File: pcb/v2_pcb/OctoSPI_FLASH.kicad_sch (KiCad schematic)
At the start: 5 parts, among them U5 MX25U51279GXDR00

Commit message: fnish micro sd card
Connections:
- net OCTOSPI_IO1: now also U5.D2 (SO/SIO1)
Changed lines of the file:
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@@
+	(wire
+		(pts
+			(xy 81.28 91.44) (xy 133.35 91.44)
+		)
+		(stroke
+			(width 0)
+			(type default)
+		)
+	)
 	(wire
 		(pts

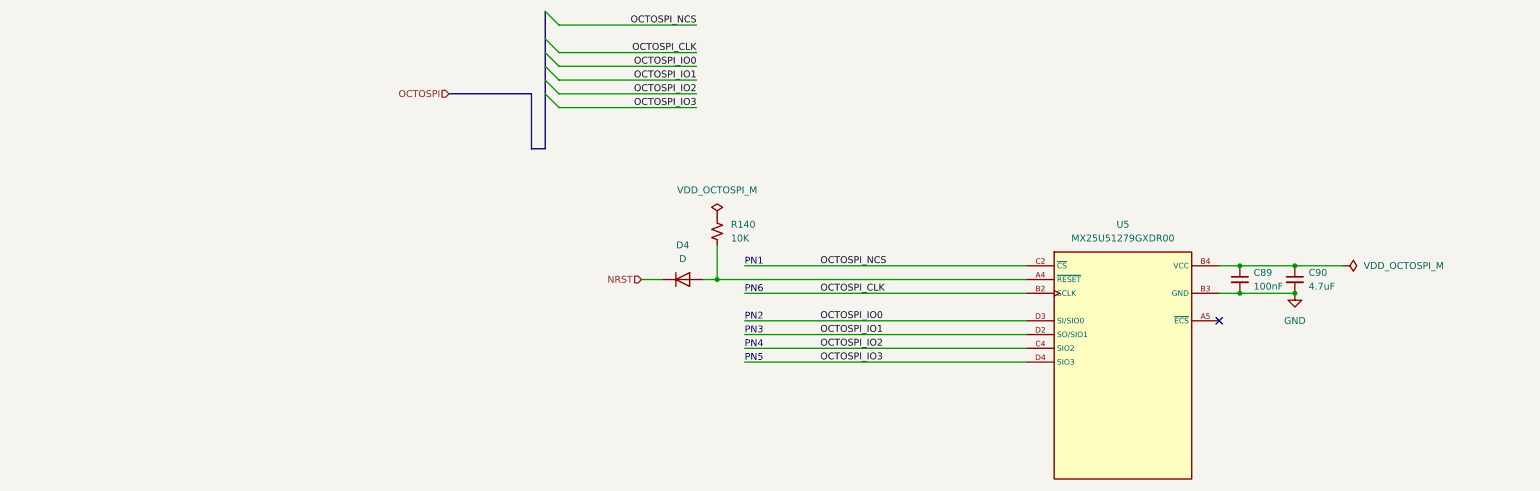
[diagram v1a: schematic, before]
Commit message: done with max17320
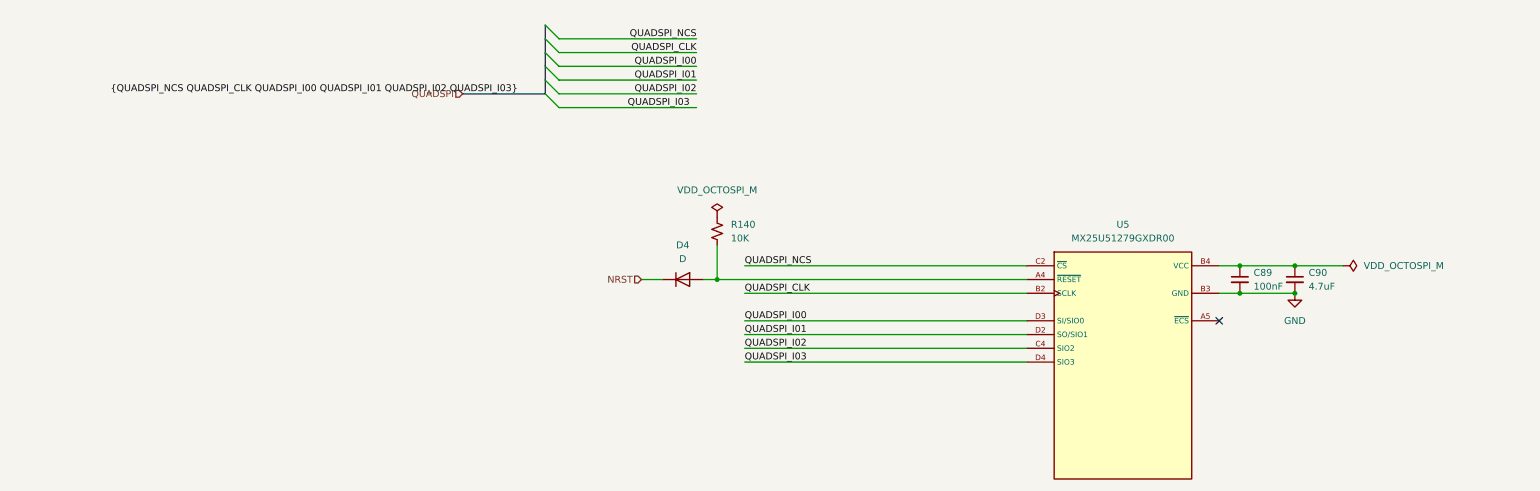
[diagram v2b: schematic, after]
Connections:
- net OCTOSPI_CLK renamed QUADSPI_CLK
- net OCTOSPI_IO0 renamed QUADSPI_I00
- net OCTOSPI_IO1 renamed QUADSPI_I01
- net OCTOSPI_IO2 renamed QUADSPI_I02
- net OCTOSPI_IO3 renamed QUADSPI_I03
- net OCTOSPI_NCS renamed QUADSPI_NCS
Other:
- note removed: "PN1"
- note removed: "PN2"
- note removed: "PN3"
- note removed: "PN4"
- note removed: "PN5"
- note removed: "PN6"
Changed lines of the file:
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@@
 	(generator_version "10.0")
 	(paper "A4")
-	(text "PN3"
-		(exclude_from_sim no)
-		(at 81.28 91.44 0)
-		(effects
-			(font
-				(size 1.27 1.27)
-			)
-			(justify left bottom)
-		)
-	)
-	(text "PN1"
-		(exclude_from_sim no)
-		(at 81.28 78.74 0)
-		(effects
-			(font
-				(size 1.27 1.27)
-			)
-			(justify left bottom)
-		)
-	)
-	(text "PN2\n"
-		(exclude_from_sim no)
-		(at 81.28 88.9 0)
-		(effects
-			(font
-				(size 1.27 1.27)
-			)
-			(justify left bottom)
-		)
-	)
-	(text "PN5"
-		(exclude_from_sim no)
-		(at 81.28 96.52 0)
-		(effects
-			(font
-				(size 1.27 1.27)
-			)
-			(justify left bottom)
-		)
-	)
-	(text "PN6\n"
-		(exclude_from_sim no)
-		(at 81.28 83.82 0)
-		(effects
-			(font
-				(size 1.27 1.27)
-			)
-			(justify left bottom)
-		)
-	)
-	(text "PN4"
-		(exclude_from_sim no)
-		(at 81.28 93.98 0)
-		(effects
-			(font
-				(size 1.27 1.27)
-			)
-			(justify left bottom)
-		)
-	)
 	(junction
 		(at 76.2 81.28)
@@
 	)
 	(bus_entry
-		(at 46.99 34.29)
-		(size -2.54 -2.54)
-		(stroke
-			(width 0)
-			(type default)
-		)
-	)
-	(wire
-		(pts
-			(xy 46.99 34.29) (xy 72.39 34.29)
+		(at 46.99 36.83)
+		(size -2.54 -2.54)
+		(stroke
+			(width 0)
+			(type default)
+		)
+	)
+	(wire
+		(pts
+			(xy 46.99 36.83) (xy 72.39 36.83)
 		)
 		(stroke
@@
 	(bus
 		(pts
-			(xy 26.67 46.99) (xy 41.91 46.99)
+			(xy 29.21 46.99) (xy 44.45 46.99)
 		)
 		(stroke
@@
 		)
 	)
+	(wire
+		(pts
+			(xy 81.28 83.82) (xy 133.35 83.82)
+		)
+		(stroke
+			(width 0)
+			(type default)
+		)
+	)
+	(wire
+		(pts
+			(xy 81.28 78.74) (xy 133.35 78.74)
+		)
+		(stroke
+			(width 0)
+			(type default)
+		)
+	)
+	(wire
+		(pts
+			(xy 62.23 81.28) (xy 66.04 81.28)
+		)
+		(stroke
+			(width 0)
+			(type default)
+		)
+	)
+	(wire
+		(pts
+			(xy 46.99 49.53) (xy 72.39 49.53)
+		)
+		(stroke
+			(width 0)
+			(type default)
+		)
+	)
+	(wire
+		(pts
+			(xy 81.28 88.9) (xy 133.35 88.9)
+		)
+		(stroke
+			(width 0)
+			(type default)
+		)
+	)
+	(wire
+		(pts
+			(xy 172.72 78.74) (xy 182.88 78.74)
+		)
+		(stroke
+			(width 0)
+			(type default)
+		)
+	)
+	(wire
+		(pts
+			(xy 46.99 46.99) (xy 72.39 46.99)
+		)
+		(stroke
+			(width 0)
+			(type default)
+		)
+	)
+	(wire
+		(pts
+			(xy 73.66 81.28) (xy 76.2 81.28)
+		)
+		(stroke
+			(width 0)
+			(type default)
+		)
+	)
 	(bus
 		(pts
-			(xy 44.45 57.15) (xy 44.45 31.75)
+			(xy 44.45 34.29) (xy 44.45 46.99)
 		)
 		(stroke
 			(width 0.508)
-			(type default)
+			(type solid)
 			(color 173 188 231 1)
 		)
@@
 	(wire
 		(pts
-			(xy 81.28 83.82) (xy 133.35 83.82)
-		)
-		(stroke
-			(width 0)
-			(type default)
-		)
-	)
-	(wire
-		(pts
-			(xy 81.28 78.74) (xy 133.35 78.74)
-		)
-		(stroke
-			(width 0)
-			(type default)
-		)
-	)
-	(wire
-		(pts
-			(xy 62.23 81.28) (xy 66.04 81.28)
-		)
-		(stroke
-			(width 0)
-			(type default)
-		)
-	)
-	(wire
-		(pts
-			(xy 46.99 49.53) (xy 72.39 49.53)
-		)
-		(stroke
-			(width 0)
-			(type default)
-		)
-	)
-	(bus
-		(pts
-			(xy 44.45 57.15) (xy 41.91 57.15)
-		)
-		(stroke
-			(width 0.508)
-			(type default)
-			(color 173 188 231 1)
-		)
-	)
-	(wire
-		(pts
-			(xy 81.28 88.9) (xy 133.35 88.9)
-		)
-		(stroke
-			(width 0)
-			(type default)
-		)
-	)
-	(wire
-		(pts
-			(xy 172.72 78.74) (xy 182.88 78.74)
-		)
-		(stroke
-			(width 0)
-			(type default)
-		)
-	)
-	(wire
-		(pts
-			(xy 46.99 46.99) (xy 72.39 46.99)
-		)
-		(stroke
-			(width 0)
-			(type default)
-		)
-	)
-	(wire
-		(pts
-			(xy 73.66 81.28) (xy 76.2 81.28)
-		)
-		(stroke
-			(width 0)
-			(type default)
-		)
-	)
-	(wire
-		(pts
 			(xy 168.91 78.74) (xy 172.72 78.74)
 		)
@@
 		)
 	)
-	(bus
-		(pts
-			(xy 41.91 57.15) (xy 41.91 46.99)
-		)
-		(stroke
-			(width 0.508)
-			(type default)
-			(color 173 188 231 1)
-		)
-	)
-	(label "OCTOSPI_IO1"
+	(label "QUADSPI_I01"
 		(at 72.39 44.45 180)
 		(effects
@@
 		)
 	)
-	(label "OCTOSPI_NCS"
-		(at 95.25 78.74 0)
-		(effects
-			(font
-				(size 1.27 1.27)
-			)
-			(justify left bottom)
-		)
-	)
-	(label "OCTOSPI_IO2"
+	(label "QUADSPI_NCS"
+		(at 81.28 78.74 0)
+		(effects
+			(font
+				(size 1.27 1.27)
+			)
+			(justify left bottom)
+		)
+	)
+	(label "{QUADSPI_NCS QUADSPI_CLK QUADSPI_I00 QUADSPI_I01 QUADSPI_I02 QUADSPI_I03}"
+		(at 39.37 46.99 180)
+		(effects
+			(font
+				(size 1.27 1.27)
+			)
+			(justify right bottom)
+		)
+	)
+	(label "QUADSPI_I02"
 		(at 72.39 46.99 180)
 		(effects
@@
 		)
 	)
-	(label "OCTOSPI_IO3"
-		(at 95.25 96.52 0)
-		(effects
-			(font
-				(size 1.27 1.27)
-			)
-			(justify left bottom)
-		)
-	)
-	(label "OCTOSPI_IO0"
-		(at 95.25 88.9 0)
-		(effects
-			(font
-				(size 1.27 1.27)
-			)
-			(justify left bottom)
-		)
-	)
-	(label "OCTOSPI_CLK"
-		(at 95.25 83.82 0)
-		(effects
-			(font
-				(size 1.27 1.27)
-			)
-			(justify left bottom)
-		)
-	)
-	(label "OCTOSPI_CLK"
+	(label "QUADSPI_I03"
+		(at 81.28 96.52 0)
+		(effects
+			(font
+				(size 1.27 1.27)
+			)
+			(justify left bottom)
+		)
+	)
+	(label "QUADSPI_I00"
+		(at 81.28 88.9 0)
+		(effects
+			(font
+				(size 1.27 1.27)
+			)
+			(justify left bottom)
+		)
+	)
+	(label "QUADSPI_CLK"
+		(at 81.28 83.82 0)
+		(effects
+			(font
+				(size 1.27 1.27)
+			)
+			(justify left bottom)
+		)
+	)
+	(label "QUADSPI_CLK"
 		(at 72.39 39.37 180)
 		(effects
@@
 		)
 	)
-	(label "OCTOSPI_NCS"
-		(at 72.39 34.29 180)
-		(effects
-			(font
-				(size 1.27 1.27)
-			)
-			(justify right bottom)
-		)
-	)
-	(label "OCTOSPI_IO0"
+	(label "QUADSPI_NCS"
+		(at 72.39 36.83 180)
+		(effects
+			(font
+				(size 1.27 1.27)
+			)
+			(justify right bottom)
+		)
+	)
+	(label "QUADSPI_I00"
 		(at 72.39 41.91 180)
 		(effects
@@
 		)
 	)
-	(label "OCTOSPI_IO1"
-		(at 95.25 91.44 0)
-		(effects
-			(font
-				(size 1.27 1.27)
-			)
-			(justify left bottom)
-		)
-	)
-	(label "OCTOSPI_IO2"
-		(at 95.25 93.98 0)
-		(effects
-			(font
-				(size 1.27 1.27)
-			)
-			(justify left bottom)
-		)
-	)
-	(label "OCTOSPI_IO3"
-		(at 72.39 49.53 180)
-		(effects
-			(font
-				(size 1.27 1.27)
-			)
-			(justify right bottom)
-		)
-	)
-	(hierarchical_label "OCTOSPI"
+	(label "QUADSPI_I01"
+		(at 81.28 91.44 0)
+		(effects
+			(font
+				(size 1.27 1.27)
+			)
+			(justify left bottom)
+		)
+	)
+	(label "QUADSPI_I02"
+		(at 81.28 93.98 0)
+		(effects
+			(font
+				(size 1.27 1.27)
+			)
+			(justify left bottom)
+		)
+	)
+	(label "QUADSPI_I03"
+		(at 71.12 49.53 180)
+		(effects
+			(font
+				(size 1.27 1.27)
+			)
+			(justify right bottom)
+		)
+	)
+	(hierarchical_label "QUADSPI"
 		(shape input)
-		(at 26.67 46.99 180)
-		(effects
-			(font
+		(at 29.21 46.99 180)
+		(effects
+			(font

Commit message: add rpls for 1v8, 5v
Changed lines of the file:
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@@
 			)
 		)
-		(property "Value" "VDD_OCTOSPI_M"
+		(property "Value" "+1V8_RUN"
 			(at 76.2 64.77 0)
 			(show_name no)
@@
 			)
 		)
-		(property "Value" "VDD_OCTOSPI_M"
+		(property "Value" "+1V8_RUN"
 			(at 195.58 78.7399 90)
 			(show_name no)

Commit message: pcb done
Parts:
- removed D4: D, symbol Device:D
- added C305: 100nF, Capacitor_SMD:C_0402_1005Metric, symbol Device:C_Small
- added D4: BAT54H, Diode_SMD:D_SOD-323, symbol Device:D_Schottky_Small
- added R303: 10k, Resistor_SMD:R_0402_1005Metric, symbol Device:R_Small_US
- C89: footprint (none) -> Capacitor_SMD:C_0402_1005Metric
- C90: footprint (none) -> Capacitor_SMD:C_0603_1608Metric
- R140: value 10K -> 10k; footprint (none) -> Resistor_SMD:R_0402_1005Metric
- U5: footprint MX66UW1G45GXDI00:BGA24C100P5X5_800X600X120 -> noob:BGA24C100P5X5_800X600X120; MPN (none) -> MX25U51279GXDR00; Manufacturer (none) -> Macronix
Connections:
- net QUADSPI_NCS is gone; now on net FLASH_NCS: U5.C2 (~{CS})
- net GND: now also C305.2
- net FLASH_NCS: now reaches R140.2
- net FLASH_NCS: no longer U5.A4 (~{RESET})
- net +1V8_RUN: now reaches C89.1, C90.1, U5.B4 (VCC)
- net +1V8_RUN: now also R140.1, D4.1 (K), R303.1
- net QUADSPI_CLK renamed FLASH_CLK
- net QUADSPI_I00 renamed FLASH_IO0
- net QUADSPI_I01 renamed FLASH_IO1
- net QUADSPI_I02 renamed FLASH_IO2
- net QUADSPI_I03 renamed FLASH_IO3
- new net FLASH_RESET_N: C305.1, D4.2 (A), R303.2, U5.A4 (~{RESET})
- no-connect marks 1 -> 15
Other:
- moved on the sheet: U5

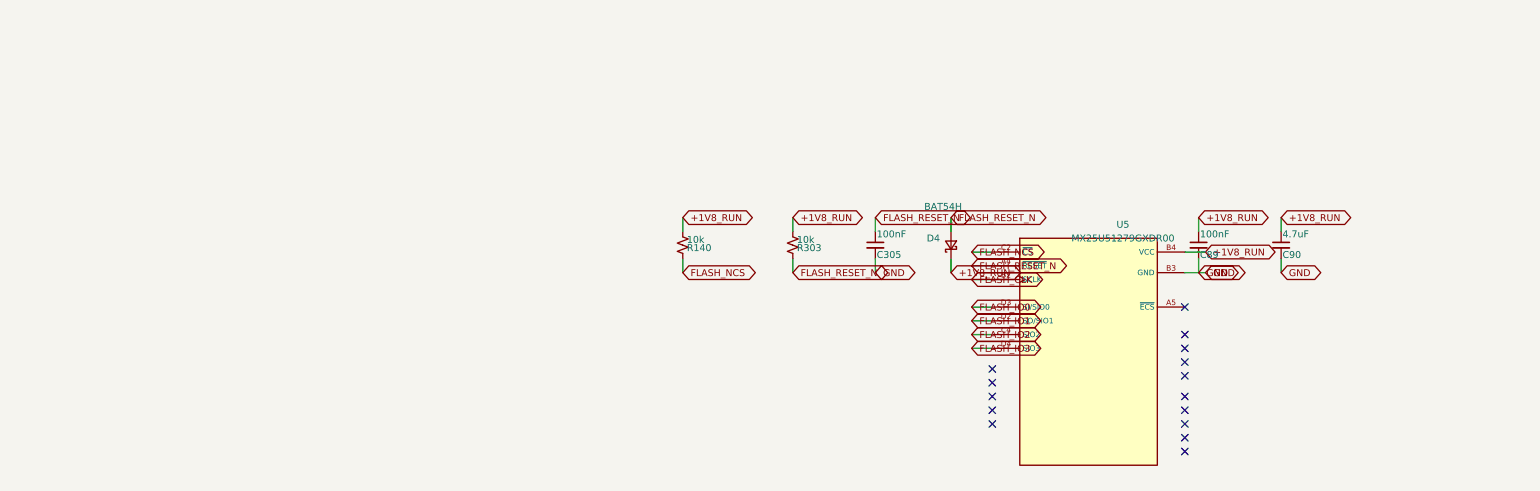
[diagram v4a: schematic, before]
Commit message: switch mosfets
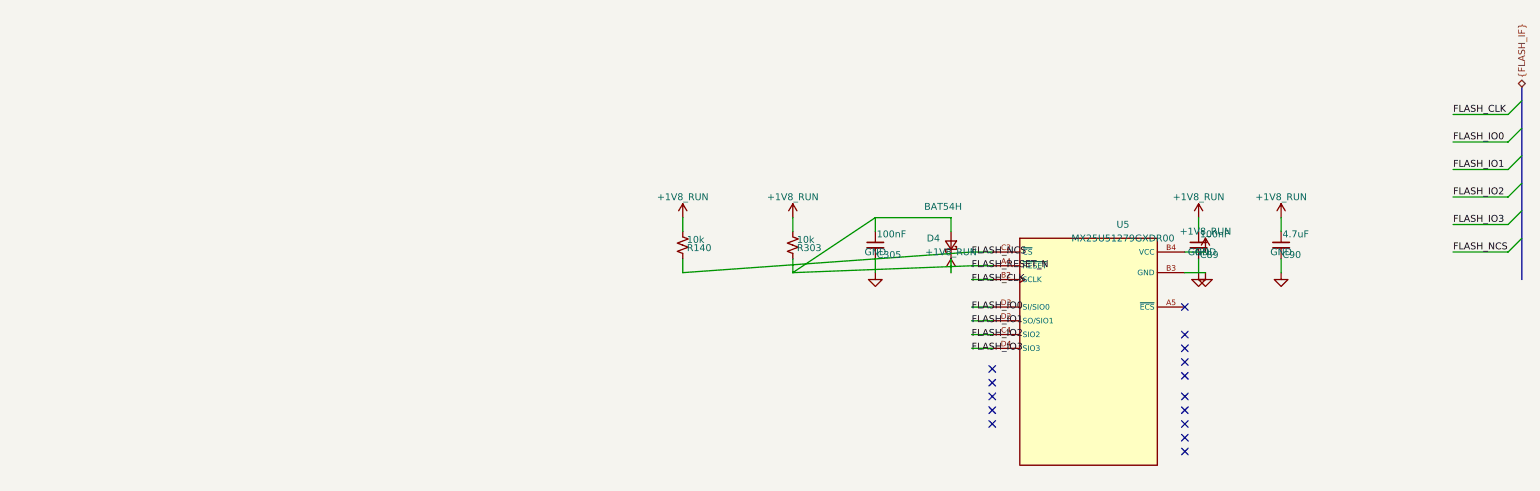
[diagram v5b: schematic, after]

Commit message: fix minor
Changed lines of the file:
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@@
 	(wire
 		(pts
-			(xy 123.19 76.2) (xy 69.85 80.01)
+			(xy 123.19 76.2) (xy 69.85 76.2)
 		)
 		(stroke
@@
 	(wire
 		(pts
-			(xy 69.85 77.47) (xy 69.85 80.01)
+			(xy 69.85 76.2) (xy 69.85 77.47)
 		)
 		(stroke
